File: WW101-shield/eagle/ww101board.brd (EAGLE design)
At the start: 59.1 x 64.6 mm, 58 parts

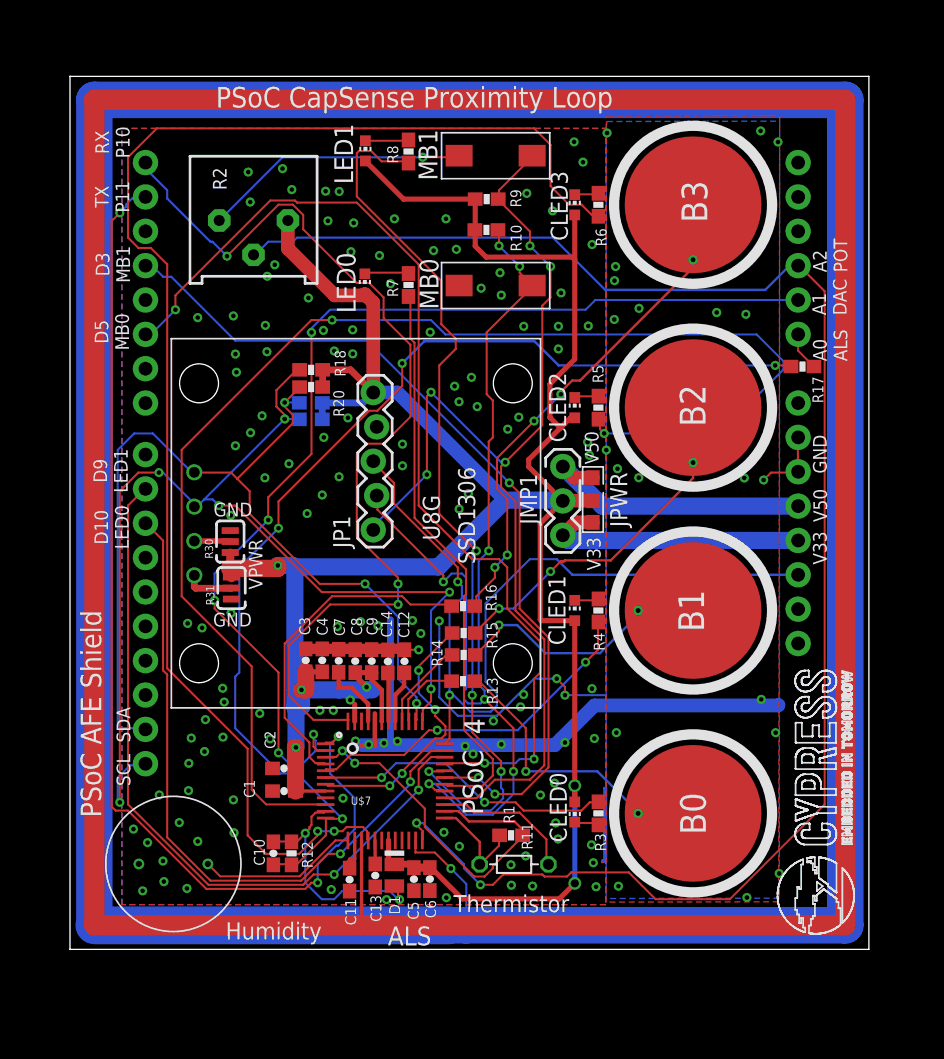
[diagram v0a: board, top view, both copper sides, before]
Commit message: Updated to latest board files and remove u8g lib from upper level.
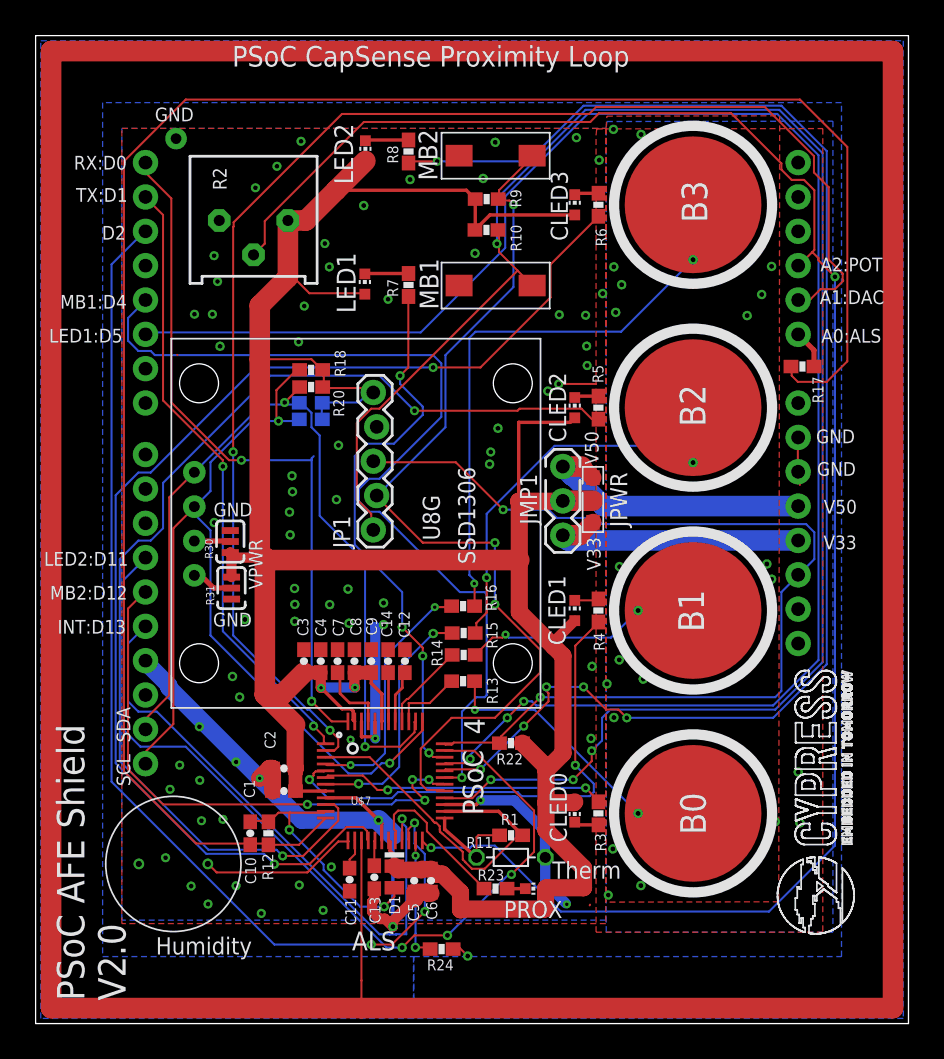
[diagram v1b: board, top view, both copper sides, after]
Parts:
- removed LED0: red, adafruit:CHIP-LED0603
- removed MB0: EVQPE1, IOTExpert:SWITCH
- added LED2, PROX: red, adafruit:CHIP-LED0603
- added MB2: EVQPE1, IOTExpert:SWITCH
- added R22: 10K, PatternAgents-ProtoPads:0603-RES
- added R23: 560, PatternAgents-ProtoPads:0603-RES
- added R24: 0R, PatternAgents-ProtoPads:0603-RES
- moved LED1 9.85 mm to (18.7, 45.6)
- moved MB1 9.60 mm to (24.7, 44.7)
- moved R12 2.27 mm to (11.6, 5.03)
- moved C10 2.27 mm to (10.3, 5.03)
- moved R11 0.56 mm to (29.5, 3.24)
- moved C3 0.15 mm to (14.2, 17.8)
- moved C6 0.15 mm to (23.6, 1.52)
- moved C13 0.14 mm to (19.4, 1.78)
- moved D1 0.13 mm to (20.9, 3.10)
- moved C4 0.12 mm to (15.5, 17.8)
- moved C5 0.11 mm to (22.4, 1.52)
- moved C7 0.09 mm to (16.7, 17.8)
- moved C8 0.06 mm to (18.0, 17.8)
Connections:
- net MBLED1 renamed LED2
- removed net D10: U$1.D10, U$7.35
- removed net D3: U$1.D3, U$7.31
- removed net D9: U$1.D9, U$7.34
- removed net MB0: JP1.2, MB0.P$2, R10.2, U$7.29
- removed net MBLED0: R7.1, U$7.30
- new net CMESH: R24.1
- new net D11: U$1.D11, U$7.35
- new net D12: U$1.D12, U$7.30
- new net D13: U$1.D13, U$7.21
- new net D4: U$1.D4, U$7.31
- new net FUTUREARD: U$1.D2, U$7.22
- new net LED1: R7.1, U$7.34
- new net MB2: JP1.2, MB2.P$2, R9.2, U$7.29
- new net N$3: PROX.C, R23.2
- new net PROXLED: R23.1, U$7.20
- net CSHIELD: now also R24.2
- net GND: now also MB2.P$1; no longer MB0.P$1
- net MB1: now also R10.2; no longer R9.2
- net N$12: now also LED1.C; no longer LED0.C
- net N$13: now also LED2.C; no longer LED1.C
- net VPWR: now also LED2.A, PROX.A, R22.1; no longer LED0.A
- net XRES: now also R22.2
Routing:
- net CSHIELD: track 241.8 -> 9.11 mm, vias 1 -> 2
- net FUTUREARD: track 0.00 -> 79.3 mm, vias 0 -> 3
- net MB0: track 76.2 -> 0.00 mm, vias 7 -> 0
- net D4: track 0.00 -> 68.8 mm, vias 0 -> 1
- net MB2: track 0.00 -> 68.2 mm, vias 0 -> 3
- net D11: track 0.00 -> 64.8 mm, vias 0 -> 3
- net D3: track 64.8 -> 0.00 mm, vias 3 -> 0
- net TIA_OUT: track 80.8 -> 141.8 mm, vias 4 -> 0
- net D9: track 54.6 -> 0.00 mm, vias 2 -> 0
- net MB1: track 78.6 -> 132.9 mm, vias 5 -> 4
- net D5: track 75.3 -> 128.6 mm
- net D10: track 50.3 -> 0.00 mm, vias 2 -> 0
- net GND: track 129.0 -> 81.6 mm, vias 151 -> 94
- net D13: track 0.00 -> 44.1 mm, vias 0 -> 1
- net MBLED0: track 42.1 -> 0.00 mm
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- added copper zone on layer 16, net CMESH
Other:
- board size 59.1 x 64.6 mm -> 64.5 x 73.1 mm
- board text added: "A0:ALS"
- board text added: "A1:DAC"
- board text added: "A2:POT"
- board text added: "D2"
- board text added: "INT:D13"
- board text added: "LED1:D5"
- board text added: "LED2:D11"
- board text added: "MB1:D4"
- board text added: "MB2"
- board text added: "MB2:D12"
- board text added: "PSoC AFE Shield V2.0"
- board text added: "PSoC Function P00 MB2/SDAT P01 MB1/SCLK P02 D12 P03 D4 P04 LED2 P05 D5 P06 LED1 P07 D11 P10 ARD-RX P11 ARD-TX"
- board text added: "PSoC Function P12 VDAC ARD-A1 P13 Therm Ref P14 CapSense B3 P15 CapLED 1 P16 CapLED 0 P17 CapSense B2 P20 CapLED 2 P21 TIAIN P22 TIAOUT ARD-A0 P23 Humidity"
- board text added: "PSoC Function P24 Humidity Ref Cap P25 Proximity P26 CapLED 3 P27 SAR Bypass P30 PROX LED P31 D13 P32 D2 P33 Prox Shield P34 Pot ARD-A3"
- board text added: "PSoC Function P35 Therm Mid P36 Therm Ref P37 Therm Low (GND) P40 SCL P41 SDA P50 CapSense B0 P51 CapSense B1 P52 CMOD P53 CTANK"
- board text added: "RX:D0"
- board text added: "TX:D1"
- board text added: "Therm"
- board text removed: "A0 ALS"
- board text removed: "A1 DAC"
- board text removed: "A2 POT"
- board text removed: "D10 LED0"
- board text removed: "D3 MB1"
- board text removed: "D5 MB0"
- board text removed: "D9 LED1"
- board text removed: "MB0"
- board text removed: "PSoC AFE Shield"
- board text removed: "PSoC Function P00 MB0 P01 MB1 P02 MBLED0 P03 ARD-D3 P04 MBLED1 P05 ARD-D5 P06 ARD-D9 P07 ARD-D10 P10 ARD-RX P11 ARD-TX"
- board text removed: "PSoC Function P12 VDAC ARD-A1 P13 THERM-REF P14 CapSense B3 P15 CapLED 1 P16 CapLED 0 P17 CapB2 P20 CapLED 2 P21 TIA-IN P22 TIAOUT ARD-A0 P23 Humidity"
- board text removed: "PSoC Function P24 Humidity Ref Cap P25 Proximity P26 CapLED 3 P27 SAR Bypass P30 Unused P31 Unused P32 Unused P33 Prox Shield P34 Pot ARD-A3"
- board text removed: "PSoC Function P35 Therm - MID P36 Therm Ref (1.2V) P37 Therm Low (GND) P40 SCL P41 SDA P50 CapSense B0 P51 CapSense B1 P52 CMOD P53 CTANK"
- board text removed: "RX P10"
- board text removed: "TX P11"
- board text removed: "Thermistor"

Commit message: Move cap on XRES to gnd, make holes larger for OLED and humidity sensor.
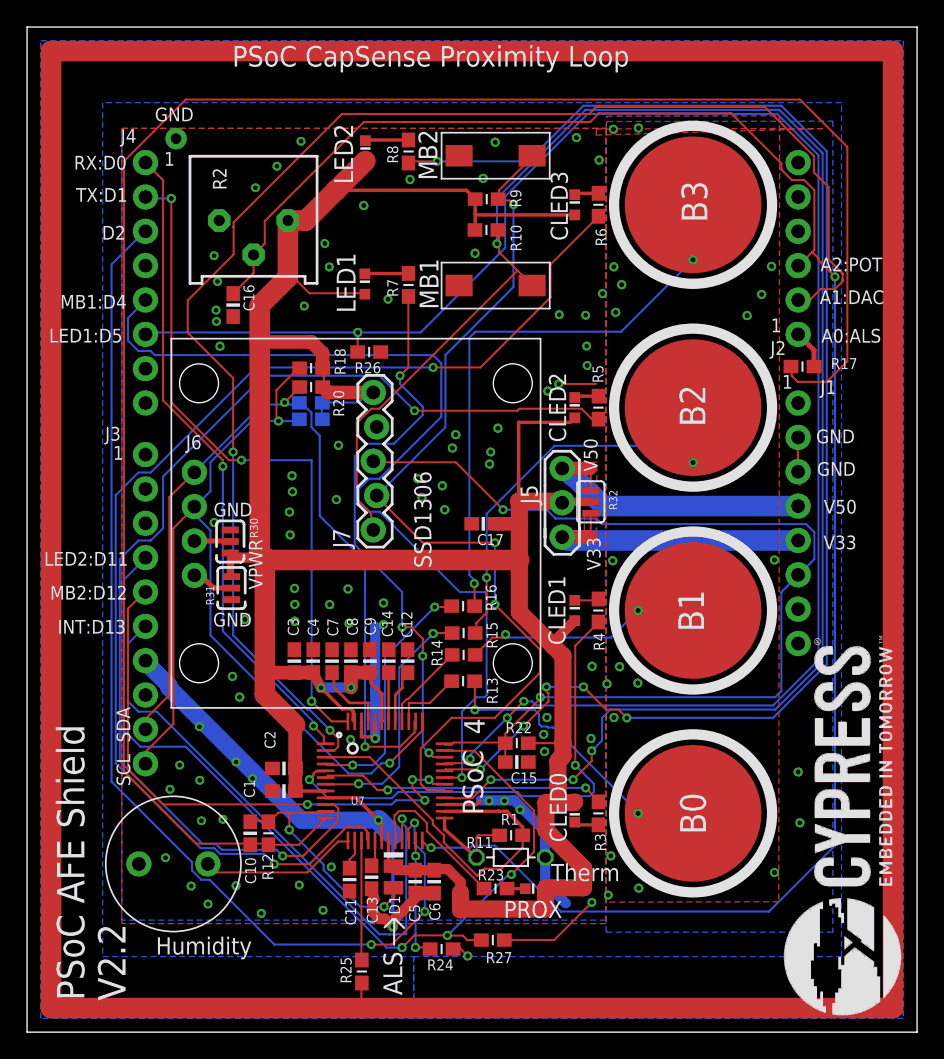
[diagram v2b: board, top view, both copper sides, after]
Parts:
- removed JMP1: 0, PatternAgents-ProtoPads:JMP-3-NO-PTH-2.54
- removed JP1: 0, SparkFun-Connectors:1X05_LOCK
- removed JPWR: 0, PatternAgents-ProtoPads:JMP-3-NO-0603
- removed U$2: U8G-096-OLED, IOTExpert:096-SSD1306
- removed U$3: (no value), IOTExpert:CYPRESSLOGO
- added C15, C16: 0.1uF, ww101board:0603-CAP
- added C17: 10uF, ww101board:0603-CAP
- added J5: (no value), ww101board:JMP-3-NO-PTH-2.54
- added J6: U8G-096-OLED, ww101board:096-SSD1306
- added J7: 0, ww101board:1X05_LOCK
- added R25: 0R, ww101board:0603-RES
- added R26, R27: 50K, ww101board:0603-RES
- added R32: (no value), ww101board:JMP-3-NO
- added U7: CY8C4A45-48, ww101board:TQFP-7X7-48
- B0, B1, B2, B3: device PatternAgents-TouchWidgets:BUTTON_PASSIVE_10MM -> ww101board:BUTTON_PASSIVE_10MM
- C1, C10, C11, C12, C13, C14, C2, C3, C4, C5, C6, C7, C8, C9: device PatternAgents-ProtoPads:0603-CAP -> ww101board:0603-CAP
- CLED0, CLED1, CLED2, CLED3, LED1, LED2, PROX: device adafruit:CHIP-LED0603 -> ww101board:CHIP-LED0603
- D1: device IOTExpert:ALS -> ww101board:ALS
- HUMIDITY: device IOTExpert:HUMIDITY -> ww101board:HUMIDITY
- MB1, MB2: device IOTExpert:SWITCH -> ww101board:SWITCH
- R1, R10, R12, R13, R14, R15, R16, R17, R22, R23, R24, R3, R4, R5, R6, R7, R8, R9: device PatternAgents-ProtoPads:0603-RES -> ww101board:0603-RES
- R11: device varistor:R-5 -> ww101board:R-5
- R18, R19, R20, R21: value 4.7K -> DNP; device PatternAgents-ProtoPads:0603-RES -> ww101board:0603-RES
- R2: device pot:3386P -> ww101board:3386P
- R30: device PatternAgents-ProtoPads:JMP-3-1_2 -> ww101board:JMP-3-1_2
- R31: device PatternAgents-ProtoPads:JMP-3-2_3 -> ww101board:JMP-3-2_3
- U$1: device SparkFun-Boards:UNO_R3_SHIELD_NOLABELS -> ww101board:UNO_R3_SHIELD_NOLABELS
- U$7: value CY8C4A45-48 -> CYLOGO-SILK; device PatternAgents-Cypress:TQFP-7X7-48 -> ww101board:CYLOGO-SILK
- moved U$7 41.9 mm to (58.4, -8.45), turned to 90 degrees
- moved C3 0.71 mm to (13.5, 17.8)
- moved C4 0.56 mm to (14.9, 17.8)
- moved R22 0.43 mm to (30.0, 11.7)
- moved C7 0.41 mm to (16.3, 17.8)
- moved C8 0.25 mm to (17.7, 17.8)
- moved C6 0.24 mm to (23.9, 1.45)
- moved C13 0.20 mm to (19.2, 1.78)
- moved C12 0.20 mm to (21.9, 17.8)
- moved R18 0.13 mm to (14.8, 39.4)
- moved C5 0.11 mm to (22.5, 1.45)
- moved C9 0.10 mm to (19.1, 17.8)
- moved D1 0.07 mm to (20.8, 3.10)
- moved C14 0.05 mm to (20.5, 17.8)
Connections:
- removed net VPWR: C1.2, C2.2, C3.2, C4.2, C5.1, C6.1, C8.2, C9.2, CLED0.A, CLED1.A, CLED2.A, CLED3.A, D1.ANNODE, JMP1.2, JP1.5, JPWR.2, LED1.A, LED2.A, PROX.A, R10.1, R18.2, R19.2, R2.3, R20.2, R21.2, R22.1, R30.1, R31.3, R9.1, U$7.19, U$7.43, U$7.47, U$7.8
- new net CAP-PSOC: R25.2, U7.15
- new net VCC: C1.2, C17.1, C2.2, C3.2, C4.2, C5.1, C6.1, C8.2, C9.2, CLED0.A, CLED1.A, CLED2.A, CLED3.A, D1.ANNODE, J5.2, J7.5, LED1.A, LED2.A, PROX.A, R10.1, R18.2, R19.2, R2.3, R20.2, R21.2, R22.1, R30.1, R31.3, R32.2, R9.1, U7.19, U7.43, U7.47, U7.8
- net CAP-PROX: now also R25.1; no longer U$7.15
- net CB0: now also U7.39; no longer U$7.39
- net CB1: now also U7.40; no longer U$7.40
- net CB2: now also U7.7; no longer U$7.7
- net CB3: now also U7.4; no longer U$7.4
- net CBLED0: now also U7.6; no longer U$7.6
- net CBLED1: now also U7.5; no longer U$7.5
- net CBLED2: now also U7.10; no longer U$7.10
- net CBLED3: now also U7.16; no longer U$7.16
- net CMOD: now also U7.41; no longer U$7.41
- net CSHIELD: now also U7.23; no longer U$7.23
- net CTANK: now also U7.42; no longer U$7.42
- net D11: now also R27.2, U7.35; no longer U$7.35
- net D12: now also U7.30; no longer U$7.30
- net D13: now also U7.21; no longer U$7.21
- net D4: now also U7.31; no longer U$7.31
- net D5: now also R26.2, U7.33; no longer U$7.33
- net FUTUREARD: now also U7.22; no longer U$7.22
- net GND: now also C15.1, C16.2, C17.2, J7.4, R26.1, R27.1, U7.18, U7.27, U7.44, U7.46, U7.9; no longer JP1.4, U$7.18, U$7.27, U$7.44, U$7.46, U$7.9
- net H-REF-CAP: now also U7.14; no longer U$7.14
- net HUMIDITY: now also U7.13; no longer U$7.13
- net LED1: now also U7.34; no longer U$7.34
- net LED2: now also U7.32; no longer U$7.32
- net MB1: now also J7.1, U7.28; no longer JP1.1, U$7.28
- net MB2: now also J7.2, U7.29; no longer JP1.2, U$7.29
- net N$14: now also J6.VDD; no longer U$2.VDD
- net N$17: now also J6.GND; no longer U$2.GND
- net N$20: now also U7.45; no longer U$7.45
- net POT: now also C16.1, U7.24; no longer U$7.24
- net PROXLED: now also U7.20; no longer U$7.20
- net SCL: now also J6.SCL, U7.37; no longer U$2.SCL, U$7.37
- net SDA: now also J6.SDA, U7.38; no longer U$2.SDA, U$7.38
- net THERM-MID: now also U7.25; no longer U$7.25
- net THERM-REF-HIGH: now also U7.26, U7.3; no longer U$7.26, U$7.3
- net TIA_IN: now also U7.11; no longer U$7.11
- net TIA_OUT: now also U7.12; no longer U$7.12
- net UARTRX: now also U7.48; no longer U$7.1
- net UARTTX: now also U7.1; no longer U$7.48
- net V33: now also J5.3, R32.1; no longer JMP1.3, JPWR.3
- net V50: now also J5.1, R32.3; no longer JMP1.1, JPWR.1
- net VDAC: now also U7.2; no longer U$7.2
- net VREF: now also U7.17; no longer U$7.17
- net XRES: now also C15.2, J7.3, U7.36; no longer JP1.3, U$7.36
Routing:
- net VCC: track 0.00 -> 215.0 mm, vias 0 -> 2
- net VPWR: track 213.5 -> 0.00 mm, vias 2 -> 0
- net CAP-PROX: track 278.4 -> 268.3 mm
- net CAP-PSOC: track 0.00 -> 8.86 mm
- net UARTRX: track 46.0 -> 50.4 mm, vias 2 -> 3
- net GND: track 81.6 -> 86.0 mm, vias 94 -> 103
- net UARTTX: track 52.2 -> 48.5 mm
- net POT: track 135.0 -> 138.5 mm
- net VDAC: track 105.2 -> 108.0 mm
- net D11: track 64.8 -> 67.5 mm
- net XRES: track 74.5 -> 76.6 mm
- net V33: track 20.2 -> 22.3 mm
- net THERM-REF-HIGH: track 26.0 -> 27.6 mm
- net D5: track 128.6 -> 130.1 mm, vias 3 -> 4
- net V50: track 21.2 -> 22.6 mm
- added copper zone on layer 1, net V33
- added copper zone on layer 1, net V50
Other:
- board size 64.5 x 73.1 mm -> 65.8 x 74.3 mm
- board text added: "1"
- board text added: "600-60500-01 REV2.2"
- board text added: "BAR CODE"
- board text added: "J1"
- board text added: "J2"
- board text added: "J3"
- board text added: "J4"
- board text added: "J6"
- board text added: "PSoC AFE Shield V2.2"
- board text added: "QR CODE"
- board text removed: "PSoC AFE Shield V2.0"
